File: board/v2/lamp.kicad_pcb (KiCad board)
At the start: 4 copper layers, 28 x 28 mm, 40 parts, among them J1 Conn_01x01_Female, J2 Conn_01x01_Female, J3 Conn_01x01_Female, J4 Conn_01x01_Female, J5 Conn_01x01_Female, J6 Conn_01x01_Female, J7 Conn_01x01_Female, J8 Conn_ARM_JTAG_SWD_10, U1 STM32L051K8Ux, U2 TLV2333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

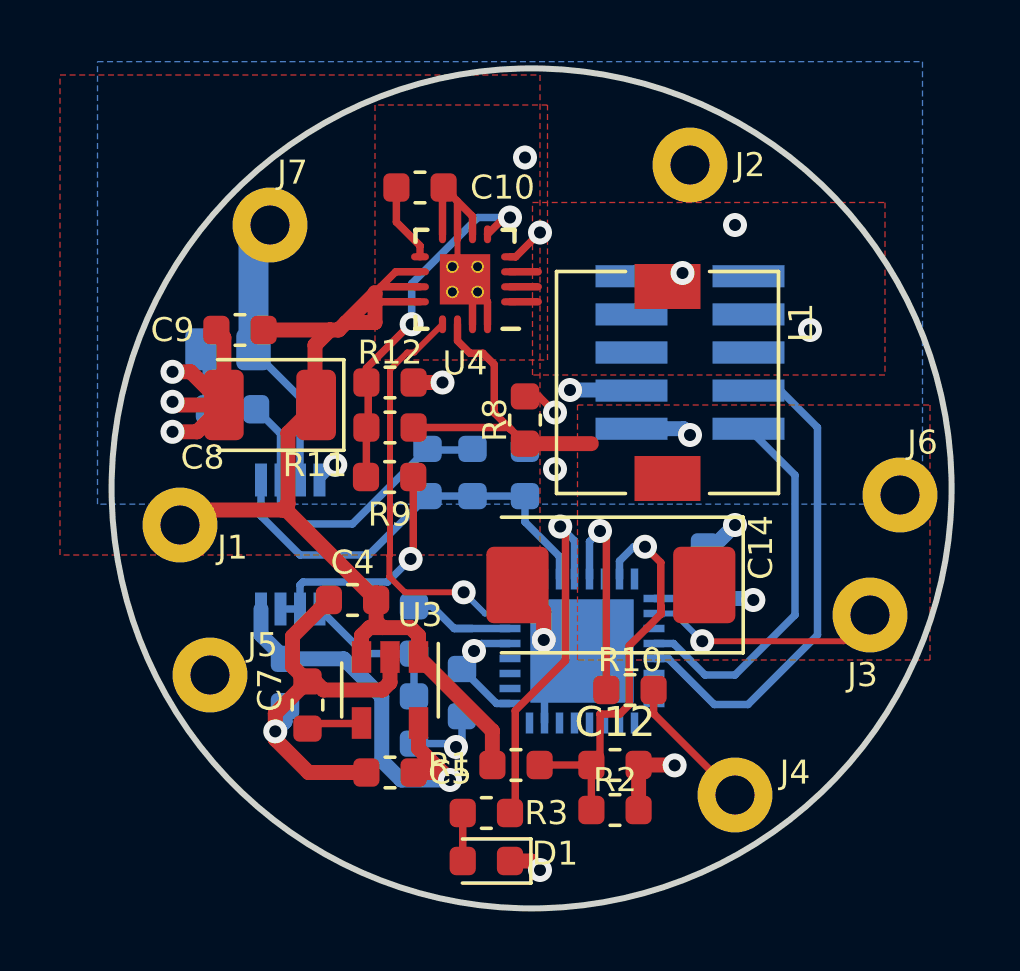
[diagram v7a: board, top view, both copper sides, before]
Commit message: board: Move to STM32G071
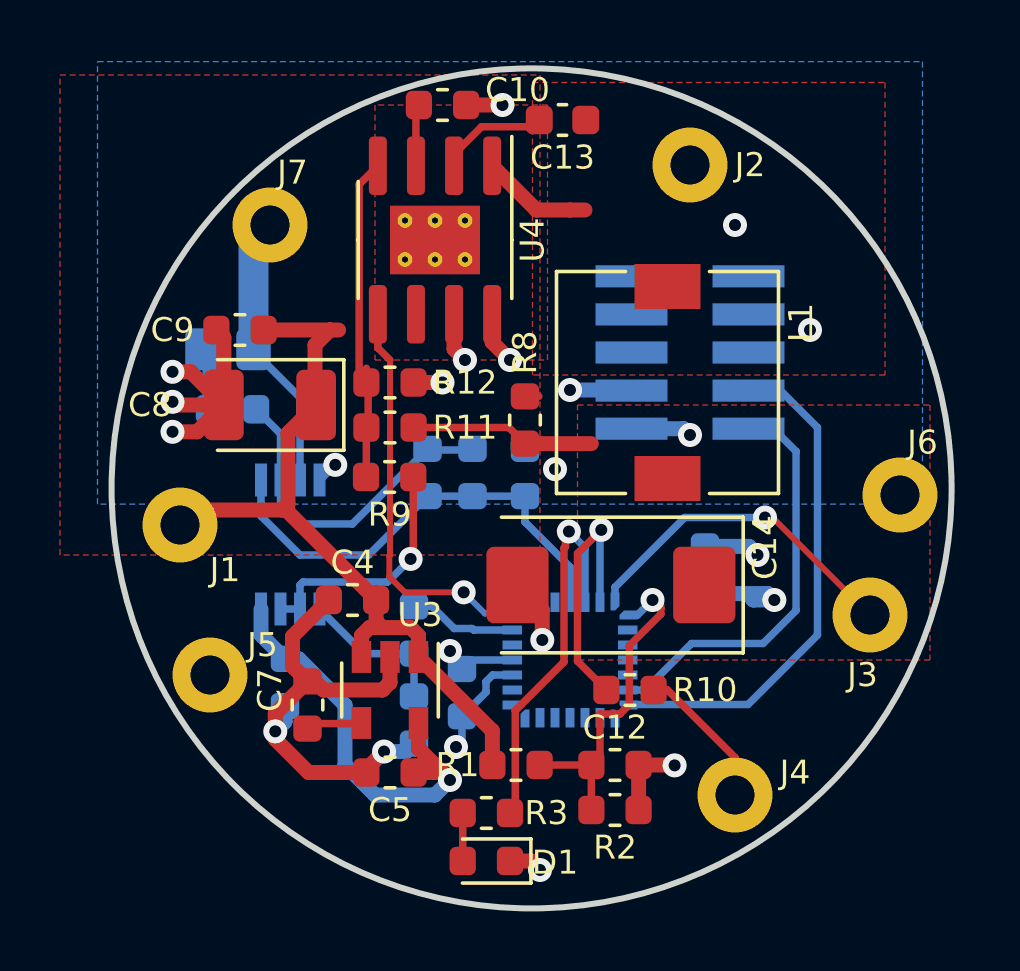
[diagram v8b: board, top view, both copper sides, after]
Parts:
- added C13: 10n, Capacitor_SMD:C_0603_1608Metric, F.Cu at (136.8, 71.5)
- U1: value STM32L051K8Ux -> STM32G071GxU; footprint Package_DFN_QFN:QFN-32-1EP_5x5mm_P0.5mm_EP3.45x3.45mm -> lamp:QFN-28_4.3x4.3_Pitch0.5mm
- U4: value TLV62130x -> LMR23625; footprint lamp:QFN-16_EP_3x3_Pitch0.5mm -> Package_SO:SOIC-8-1EP_3.9x4.9mm_P1.27mm_EP2.29x3mm_ThermalVias
- moved C10 2.85 mm to (132.8, 71.0)
- moved U4 1.65 mm to (132.5, 75.5), turned to -90 degrees
- moved U1 0.50 mm to (137.0, 89.5)
- turned C2 to 90 degrees
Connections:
- net /VBAT renamed /VBAT_SENSE
- U1 pad 1: +3V3 -> unconnected-(U1-Pad1)
- U1 pad 14: unconnected-(U1-Pad14) -> /BTN
- U1 pad 17: +3V3 -> unconnected-(U1-Pad17)
- U1 pad 18: /BTN -> unconnected-(U1-Pad18)
- U1 pad 3: unconnected-(U1-Pad3) -> +3V3
- U1 pad 4: /RESET -> GND
- U1 pad 5: +3V3 -> /RESET
- U4 pad 2: /SW -> Net-(C13-Pad1)
- U4 pad 3: /SW -> Net-(C10-Pad1)
- U4 pad 4: /PWRGD -> Net-(R11-Pad2)
- U4 pad 5: Net-(R11-Pad2) -> /EN
- U4 pad 6: GND -> unconnected-(U4-Pad6)
- U4 pad 7: GND -> /VIN
- U4 pad 9: Net-(C10-Pad1) -> GND
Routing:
- net GND: track 51.3 -> 42.7 mm, vias 17 -> 18
- net /PWRGD: track 9.02 -> 0.71 mm, vias 2 -> 0
- net /VIN: track 34.6 -> 27.4 mm, vias 0 -> 1
- net /LED_P: track 10.7 -> 6.15 mm
- net Net-(C13-Pad1): track 0.00 -> 3.70 mm
- net /VBAT_SENSE: track 14.3 -> 10.9 mm
- net /BTN: track 7.95 -> 11.3 mm
- net /LED2: track 7.90 -> 9.32 mm
- net Net-(R11-Pad2): track 12.3 -> 11.2 mm, vias 2 -> 0
- net /ISENSE_BUFD: track 14.6 -> 15.5 mm
- net /SW: track 2.82 -> 3.71 mm
- net Net-(J4-Pad1): track 5.47 -> 4.89 mm
- net Net-(C10-Pad1): track 2.64 -> 2.07 mm
- net /SETPOINT_PWM: track 4.11 -> 3.60 mm
- added copper zone on In2.Cu, net /VIN
